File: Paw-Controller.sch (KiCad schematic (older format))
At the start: 26 parts, among them J1 Conn_02x06_Odd_Even, J2 Conn_01x08, J3 Conn_01x02, Q1 DMN1019USN, Q2 DMN1019USN, Q3 DMN1019USN, SW1 SW_SPST_KMR2, U1 LMZ10503, U2 ATSAMD21E18A-AF

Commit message: Added missing PWM labels.
Signed-off-by: Aaron Williams <aaron.w2@gmail.com>
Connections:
- net labels added: PWM0, PWM1, PWM2
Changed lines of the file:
@@
 Wire Notes Line
 	6200 4600 10300 4600
+Text Label 8100 2600 0    50   ~ 0
+PWM0
+Text Label 8100 2700 0    50   ~ 0
+PWM1
+Text Label 8850 3300 0    50   ~ 0
+PWM2
 $EndSCHEMATC

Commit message: Version 2.0 converts each PWM channel to use an H-bridge.
This allows the controller to be able to drive a 3V brushless motor.  The
M0 processor is capable of generating the timing for the motors, though at
this time I don't know if it works with 6 GPIO pins or only with three.

Six was chosen so that a PWMs can be set to a high impedence state.  This
is useful in the case where multiple brushed motors are attached between either
+3v or ground and the PWM pin, though the alternative is to just pull the PWM
output to the same level.  That might be version 2.1 later.

Signed-off-by: Aaron Williams <aaron.w2@gmail.com>
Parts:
- removed D1, D2, D3: B120-E3, Diode_SMD:D_SMA, symbol Diode:B120-E3
- added Q4, Q5, Q6: SI3493DDV-T1-GE3, Package_SO:TSOP-6_1.65x3.05mm_P0.95mm, symbol Aaron:SI3493DDV-T1-GE3
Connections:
- net labels added: PA03, PA04, PA05
- wire segments 85 -> 90
- no-connect marks 14 -> 12
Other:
- note added: "PWM Drivers, 3V Max"
- note removed: "PWM Drivers, 5V Max"
- moved on the sheet: C8, Q1, Q2, Q3, SW1

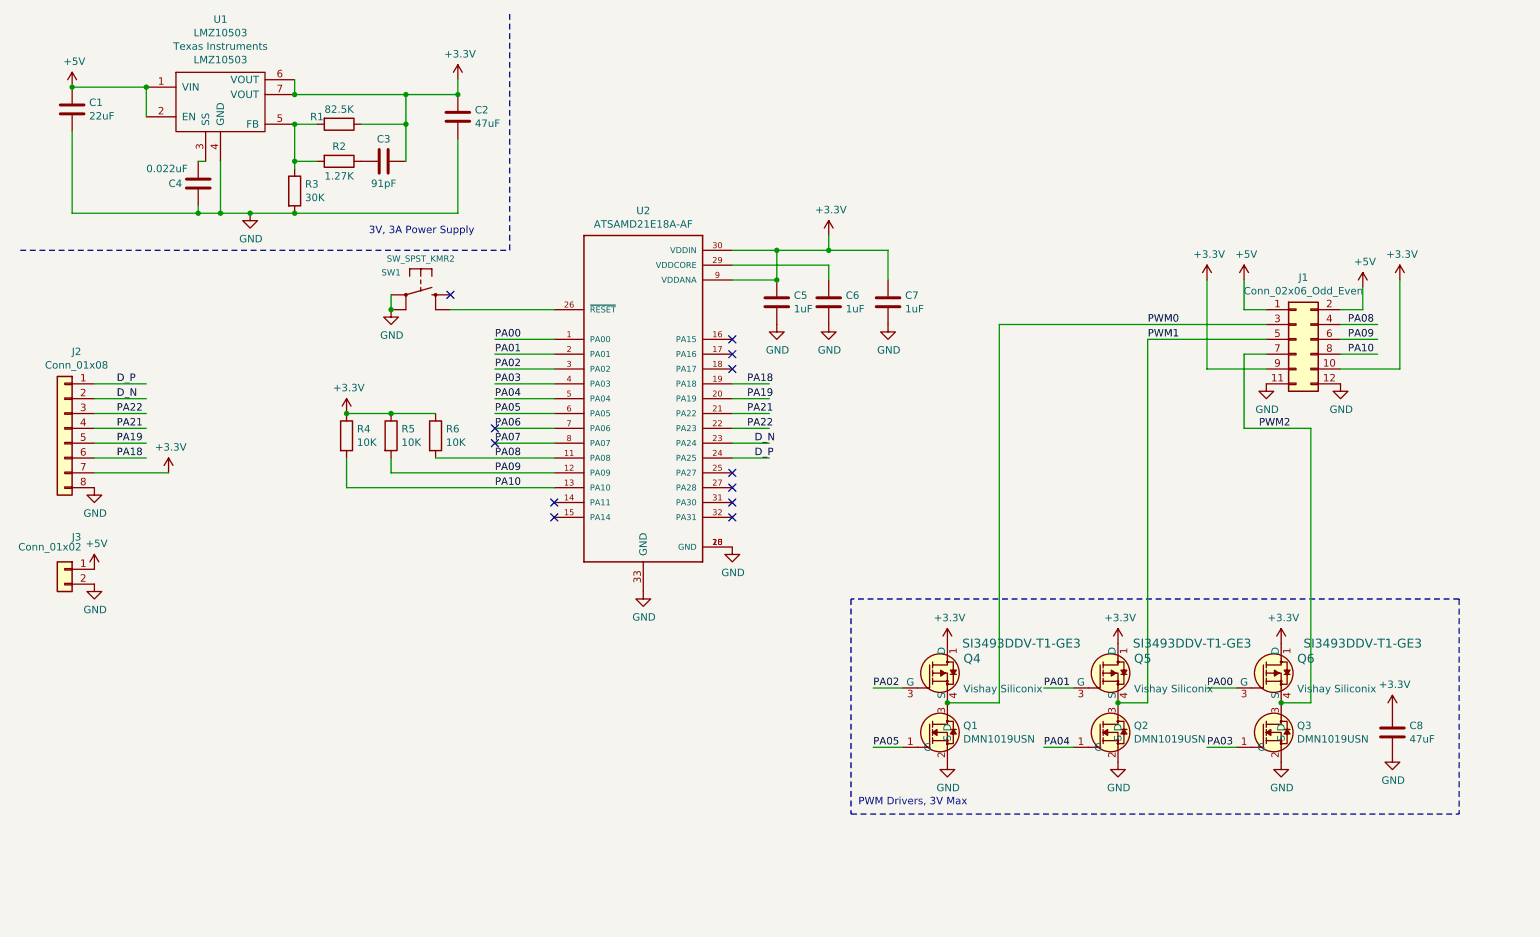
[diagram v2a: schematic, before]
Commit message: Fixed solder mask clearance.
Signed-off-by: Aaron Williams <aaron.w2@gmail.com>
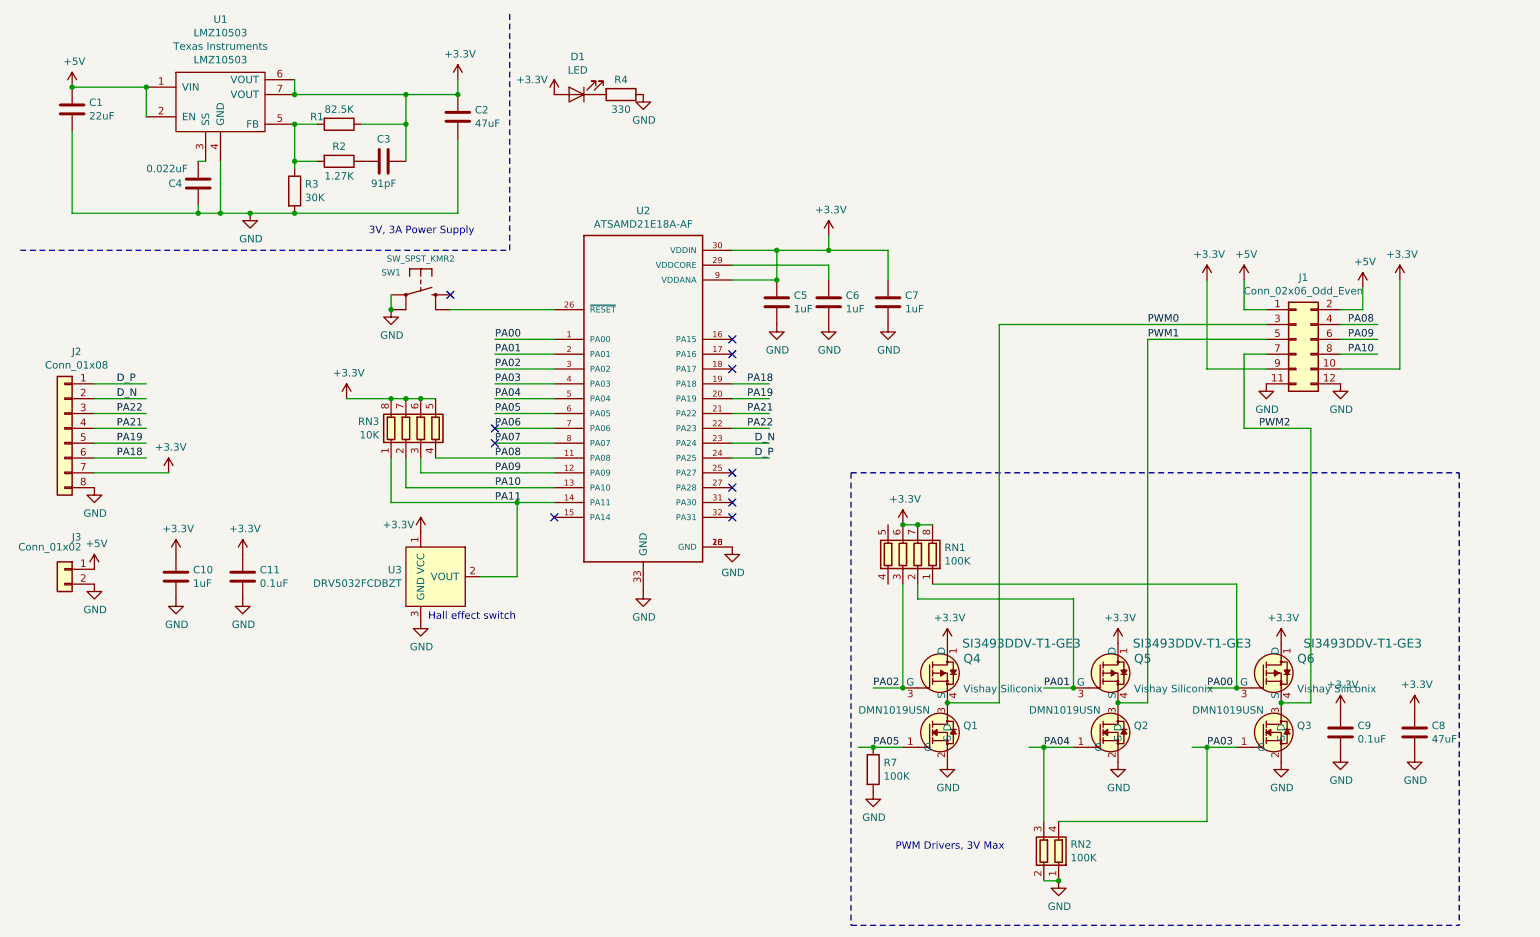
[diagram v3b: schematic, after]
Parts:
- removed R5, R6: 10K, Resistor_SMD:R_0603_1608Metric, symbol Device:R
- added C10: 1uF, Capacitor_SMD:C_0603_1608Metric, symbol Device:C
- added C11, C9: 0.1uF, Capacitor_SMD:C_0603_1608Metric, symbol Device:C
- added D1: LED, LED_SMD:LED_0603_1608Metric, symbol Device:LED
- added R7: 100K, Resistor_SMD:R_0603_1608Metric, symbol Paw-Controller-rescue:R-device
- added RN1: 100K, Resistor_SMD:R_Array_Convex_4x0603, symbol Paw-Controller-rescue:R_Pack04-device
- added RN2: 100K, Resistor_SMD:R_Array_Convex_2x0603, symbol Paw-Controller-rescue:R_Pack02-device
- added RN3: 10K, Resistor_SMD:R_Array_Convex_4x0603, symbol Paw-Controller-rescue:R_Pack04-device
- added U3: DRV5032FCDBZT, Package_TO_SOT_SMD:SOT-23, symbol Aaron:DRV5032FCDBZT
- R4: value 10K -> 330
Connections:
- net labels added: PA11
- wire segments 90 -> 112
- no-connect marks 12 -> 11
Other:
- note added: "Hall effect switch"
- moved on the sheet: C8

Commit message: Fixed P-CH mosfets and changed to more readily available mosfet.
Signed-off-by: Aaron Williams <aaron.w2@gmail.com>
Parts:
- removed Q4, Q5, Q6: SI3493DDV-T1-GE3, Package_SO:TSOP-6_1.65x3.05mm_P0.95mm, symbol Aaron:SI3493DDV-T1-GE3
- added Q? (x3): SI3407DV-T1-GE3, digikey-footprints:SOT-23-3, symbol Aaron:SI3407DV-T1-GE3
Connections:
- wire segments 112 -> 115
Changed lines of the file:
@@
 Sheet 1 1
 Title "3v PWM controller"
-Date "2018-10-16"
-Rev "2.1"
+Date "2019-01-29"
+Rev "2.1.2"
 Comp "Aaron Williams"
 Comment1 ""
@@
 Text Label 8850 3300 0    50   ~ 0
 PWM2
-$Comp
-L Aaron:SI3493DDV-T1-GE3 Q4
-U 1 1 5BC63C22
-P 6750 4950
-F 0 "Q4" H 6858 5048 60  0000 L CNN
-F 1 "SI3493DDV-T1-GE3" H 6850 5150 60  0000 L CNN
-F 2 "Package_SO:TSOP-6_1.65x3.05mm_P0.95mm" H 6950 5150 60  0001 L CNN
-F 3 "http://www.vishay.com/docs/74735/si3493ddv.pdf" H 6950 5250 60  0001 L CNN
-F 4 "Vishay Siliconix" H 6858 4844 50  0000 L CNN "MFR"
-F 5 "SI3493DDV-T1-GE3" H 6950 5450 60  0001 L CNN "MPN"
-F 6 "SI3493DDV-T1-GE3TR-ND" H 6950 5350 60  0001 L CNN "Digi-Key_PN"
-F 7 "Discrete Semiconductor Products" H 6950 5550 60  0001 L CNN "Category"
-F 8 "Transistors - FETs, MOSFETs - Single" H 6950 5650 60  0001 L CNN "Family"
-F 9 "http://www.vishay.com/docs/74735/si3493ddv.pdf" H 6950 5750 60  0001 L CNN "DK_Datasheet_Link"
-F 10 "https://www.digikey.com/product-detail/en/vishay-siliconix/SI3493DDV-T1-GE3/" H 6950 5850 60  0001 L CNN "DK_Detail_Page"
-F 11 "MOSFET P-CH 20V 8A 6TSOP" H 6950 5950 60  0001 L CNN "Description"
-F 12 "Vishay Siliconix" H 6950 6050 60  0001 L CNN "Manufacturer"
-F 13 "Active" H 6950 6150 60  0001 L CNN "Status"
-	1    6750 4950
-	1    0    0    -1
-$EndComp
-$Comp
-L Aaron:SI3493DDV-T1-GE3 Q5
-U 1 1 5BC646E4
-P 7900 4950
-F 0 "Q5" H 8008 5048 60  0000 L CNN
-F 1 "SI3493DDV-T1-GE3" H 8000 5150 60  0000 L CNN
-F 2 "Package_SO:TSOP-6_1.65x3.05mm_P0.95mm" H 8100 5150 60  0001 L CNN
-F 3 "http://www.vishay.com/docs/74735/si3493ddv.pdf" H 8100 5250 60  0001 L CNN
-F 4 "Vishay Siliconix" H 8008 4844 50  0000 L CNN "MFR"
-F 5 "SI3493DDV-T1-GE3" H 8100 5450 60  0001 L CNN "MPN"
-F 6 "SI3493DDV-T1-GE3TR-ND" H 8100 5350 60  0001 L CNN "Digi-Key_PN"
-F 7 "Discrete Semiconductor Products" H 8100 5550 60  0001 L CNN "Category"
-F 8 "Transistors - FETs, MOSFETs - Single" H 8100 5650 60  0001 L CNN "Family"
-F 9 "http://www.vishay.com/docs/74735/si3493ddv.pdf" H 8100 5750 60  0001 L CNN "DK_Datasheet_Link"
-F 10 "https://www.digikey.com/product-detail/en/vishay-siliconix/SI3493DDV-T1-GE3/" H 8100 5850 60  0001 L CNN "DK_Detail_Page"
-F 11 "MOSFET P-CH 20V 8A 6TSOP" H 8100 5950 60  0001 L CNN "Description"
-F 12 "Vishay Siliconix" H 8100 6050 60  0001 L CNN "Manufacturer"
-F 13 "Active" H 8100 6150 60  0001 L CNN "Status"
-	1    7900 4950
-	1    0    0    -1
-$EndComp
-$Comp
-L Aaron:SI3493DDV-T1-GE3 Q6
-U 1 1 5BC647C5
-P 9000 4950
-F 0 "Q6" H 9108 5048 60  0000 L CNN
-F 1 "SI3493DDV-T1-GE3" H 9150 5150 60  0000 L CNN
-F 2 "Package_SO:TSOP-6_1.65x3.05mm_P0.95mm" H 9200 5150 60  0001 L CNN
-F 3 "http://www.vishay.com/docs/74735/si3493ddv.pdf" H 9200 5250 60  0001 L CNN
-F 4 "Vishay Siliconix" H 9108 4844 50  0000 L CNN "MFR"
-F 5 "SI3493DDV-T1-GE3" H 9200 5450 60  0001 L CNN "MPN"
-F 6 "SI3493DDV-T1-GE3TR-ND" H 9200 5350 60  0001 L CNN "Digi-Key_PN"
-F 7 "Discrete Semiconductor Products" H 9200 5550 60  0001 L CNN "Category"
-F 8 "Transistors - FETs, MOSFETs - Single" H 9200 5650 60  0001 L CNN "Family"
-F 9 "http://www.vishay.com/docs/74735/si3493ddv.pdf" H 9200 5750 60  0001 L CNN "DK_Datasheet_Link"
-F 10 "https://www.digikey.com/product-detail/en/vishay-siliconix/SI3493DDV-T1-GE3/" H 9200 5850 60  0001 L CNN "DK_Detail_Page"
-F 11 "MOSFET P-CH 20V 8A 6TSOP" H 9200 5950 60  0001 L CNN "Description"
-F 12 "Vishay Siliconix" H 9200 6050 60  0001 L CNN "Manufacturer"
-F 13 "Active" H 9200 6150 60  0001 L CNN "Status"
-	1    9000 4950
-	1    0    0    -1
-$EndComp
 Wire Wire Line
 	6450 5050 6250 5050
@@
 Wire Wire Line
 	7100 5150 7100 2600
-Connection ~ 6750 5150
 Wire Wire Line
 	7100 2600 8900 2600
@@
 Wire Wire Line
 	8100 5150 8100 2700
-Connection ~ 7900 5150
 Wire Wire Line
 	9000 5150 9200 5150
@@
 Wire Wire Line
 	8750 3300 9200 3300
-Connection ~ 9000 5150
 $Comp
 L power:+3.3V #PWR025
@@
 	-1   0    0    -1
 $EndComp
-Connection ~ 8700 5050
 Wire Wire Line
 	6550 4350 6550 4450
-Wire Wire Line
-	7600 4450 7600 5050
-Connection ~ 7600 5050
-Connection ~ 6450 5050
 Wire Wire Line
 	6250 5450 6450 5450
@@
 $EndComp
 Wire Wire Line
-	8700 4350 8700 5050
-Wire Wire Line
 	6450 3950 6550 3950
 Connection ~ 6450 3950
@@
 Wire Wire Line
 	6550 4450 7600 4450
-Wire Wire Line
-	6450 4350 6450 5050
 Wire Notes Line
 	6100 3600 10200 3600
@@
 Text Notes 3250 4600 0    50   ~ 0
 Hall effect switch
+$Comp
+L Aaron:SI3407DV-T1-GE3 Q?
+U 1 1 5C524C33
+P 6750 4950
+F 0 "Q?" H 6858 4897 60  0000 L CNN
+F 1 "SI3407DV-T1-GE3" H 6550 4750 60  0000 L CNN
+F 2 "digikey-footprints:SOT-23-3" H 6950 5150 60  0001 L CNN
+F 3 "http://www.vishay.com/docs/74735/si3493ddv.pdf" H 6950 5250 60  0001 L CNN
+F 4 "Vishay Siliconix" H 7250 5050 50  0001 C CNN "MFR"
+F 5 "SI3407DV-T1-GE3" H 6950 5450 60  0001 L CNN "MPN"
+F 6 "Digikey" H 6944 5393 50  0001 C CNN "SPR"
+F 7 "SI3407DV-T1-GE3CT-ND" H 7044 5493 50  0001 C CNN "SPN"
+F 8 "https://www.digikey.com/product-detail/en/vishay-siliconix/SI3407DV-T1-GE3/SI3407DV-T1-GE3CT-ND/" H 7144 5593 50  0001 C CNN "SPURL"
+F 9 "SI3407DV-T1-GE3TR-ND" H 6950 5350 60  0001 L CNN "Digi-Key_PN"
+F 10 "Discrete Semiconductor Products" H 6950 5550 60  0001 L CNN "Category"
+F 11 "Transistors - FETs, MOSFETs - Single" H 6950 5650 60  0001 L CNN "Family"
+F 12 "http://www.vishay.com/docs/69987/si3407dv.pdf" H 6950 5750 60  0001 L CNN "DK_Datasheet_Link"
+F 13 "https://www.digikey.com/product-detail/en/vishay-siliconix/SI3407DV-T1-GE3/SI3407DV-T1-GE3CT-ND/" H 6950 5850 60  0001 L CNN "DK_Detail_Page"
+F 14 "MOSFET P-CH 20V 8A 6TSOP" H 6950 5950 60  0001 L CNN "Description"
+F 15 "Vishay Siliconix" H 6950 6050 60  0001 L CNN "Manufacturer"
+F 16 "Active" H 6950 6150 60  0001 L CNN "Status"
+	1    6750 4950
+	1    0    0    1
+$EndComp
+Wire Wire Line
+	6450 4350 6450 4850
+Connection ~ 6450 4850
+Wire Wire Line
+	6450 4850 6450 5050
+Connection ~ 6750 5150
+Wire Wire Line
+	7600 4450 7600 4850
+$Comp
+L Aaron:SI3407DV-T1-GE3 Q?
+U 1 1 5C534FFC
+P 7900 4950
+F 0 "Q?" H 8008 4897 60  0000 L CNN
+F 1 "SI3407DV-T1-GE3" H 7700 4750 60  0000 L CNN
+F 2 "digikey-footprints:SOT-23-3" H 8100 5150 60  0001 L CNN
+F 3 "http://www.vishay.com/docs/74735/si3493ddv.pdf" H 8100 5250 60  0001 L CNN
+F 4 "Vishay Siliconix" H 8400 5050 50  0001 C CNN "MFR"
+F 5 "SI3407DV-T1-GE3" H 8100 5450 60  0001 L CNN "MPN"
+F 6 "Digikey" H 8094 5393 50  0001 C CNN "SPR"
+F 7 "SI3407DV-T1-GE3CT-ND" H 8194 5493 50  0001 C CNN "SPN"
+F 8 "https://www.digikey.com/product-detail/en/vishay-siliconix/SI3407DV-T1-GE3/SI3407DV-T1-GE3CT-ND/" H 8294 5593 50  0001 C CNN "SPURL"
+F 9 "SI3407DV-T1-GE3TR-ND" H 8100 5350 60  0001 L CNN "Digi-Key_PN"
+F 10 "Discrete Semiconductor Products" H 8100 5550 60  0001 L CNN "Category"
+F 11 "Transistors - FETs, MOSFETs - Single" H 8100 5650 60  0001 L CNN "Family"
+F 12 "http://www.vishay.com/docs/69987/si3407dv.pdf" H 8100 5750 60  0001 L CNN "DK_Datasheet_Link"
+F 13 "https://www.digikey.com/product-detail/en/vishay-siliconix/SI3407DV-T1-GE3/SI3407DV-T1-GE3CT-ND/" H 8100 5850 60  0001 L CNN "DK_Detail_Page"
+F 14 "MOSFET P-CH 20V 8A 6TSOP" H 8100 5950 60  0001 L CNN "Description"
+F 15 "Vishay Siliconix" H 8100 6050 60  0001 L CNN "Manufacturer"
+F 16 "Active" H 8100 6150 60  0001 L CNN "Status"
+	1    7900 4950
+	1    0    0    1
+$EndComp
+Connection ~ 7900 5150
+Connection ~ 7600 4850
+Wire Wire Line
+	7600 4850 7600 5050
+Wire Wire Line
+	8700 4350 8700 4850
+$Comp
+L Aaron:SI3407DV-T1-GE3 Q?
+U 1 1 5C535C5D
+P 9000 4950
+F 0 "Q?" H 9108 4897 60  0000 L CNN
+F 1 "SI3407DV-T1-GE3" H 8800 4750 60  0000 L CNN
+F 2 "digikey-footprints:SOT-23-3" H 9200 5150 60  0001 L CNN
+F 3 "http://www.vishay.com/docs/74735/si3493ddv.pdf" H 9200 5250 60  0001 L CNN
+F 4 "Vishay Siliconix" H 9500 5050 50  0001 C CNN "MFR"
+F 5 "SI3407DV-T1-GE3" H 9200 5450 60  0001 L CNN "MPN"
+F 6 "Digikey" H 9194 5393 50  0001 C CNN "SPR"
+F 7 "SI3407DV-T1-GE3CT-ND" H 9294 5493 50  0001 C CNN "SPN"
+F 8 "https://www.digikey.com/product-detail/en/vishay-siliconix/SI3407DV-T1-GE3/SI3407DV-T1-GE3CT-ND/" H 9394 5593 50  0001 C CNN "SPURL"
+F 9 "SI3407DV-T1-GE3TR-ND" H 9200 5350 60  0001 L CNN "Digi-Key_PN"
+F 10 "Discrete Semiconductor Products" H 9200 5550 60  0001 L CNN "Category"
+F 11 "Transistors - FETs, MOSFETs - Single" H 9200 5650 60  0001 L CNN "Family"
+F 12 "http://www.vishay.com/docs/69987/si3407dv.pdf" H 9200 5750 60  0001 L CNN "DK_Datasheet_Link"
+F 13 "https://www.digikey.com/product-detail/en/vishay-siliconix/SI3407DV-T1-GE3/SI3407DV-T1-GE3CT-ND/" H 9200 5850 60  0001 L CNN "DK_Detail_Page"
+F 14 "MOSFET P-CH 20V 8A 6TSOP" H 9200 5950 60  0001 L CNN "Description"
+F 15 "Vishay Siliconix" H 9200 6050 60  0001 L CNN "Manufacturer"
+F 16 "Active" H 9200 6150 60  0001 L CNN "Status"
+	1    9000 4950
+	1    0    0    1
+$EndComp
+Connection ~ 9000 5150
+Connection ~ 8700 4850
+Wire Wire Line
+	8700 4850 8700 5050
 $EndSCHEMATC

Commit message: Add another push/pull channel
This adds a 4th push/pull channel and exports PA17 to J1.

Due to the increase in board size, two more pins were added to J2,
an additional +5 and ground pin for USB.

Updated to version 2.2.0

Signed-off-by: Aaron Williams <aaron.w2@gmail.com>
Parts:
- removed J1: Conn_02x06_Odd_Even, Connector_PinHeader_2.54mm:PinHeader_2x06_P2.54mm_Vertical, symbol Connector_Generic:Conn_02x06_Odd_Even
- removed J2: Conn_01x08, Connector_PinHeader_2.54mm:PinHeader_1x08_P2.54mm_Vertical, symbol Connector_Generic:Conn_01x08
- removed R7: 100K, Resistor_SMD:R_0603_1608Metric, symbol Paw-Controller-rescue:R-device
- removed RN2: 100K, Resistor_SMD:R_Array_Convex_2x0603, symbol Paw-Controller-rescue:R_Pack02-device
- added J1: Conn_02x07_Odd_Even, Connector_PinHeader_2.54mm:PinHeader_2x07_P2.54mm_Vertical, symbol Connector_Generic:Conn_02x07_Odd_Even
- added J2: Conn_01x10, Connector_PinHeader_2.54mm:PinHeader_1x10_P2.54mm_Vertical, symbol Connector_Generic:Conn_01x10
- added Q7: SI3407DV-T1-GE3, Package_SO:TSOP-6_1.65x3.05mm_P0.95mm, symbol Aaron:SI3407DV-T1-GE3
- added Q8: DMN1019USN, Package_TO_SOT_SMD:SOT-23, symbol Aaron:DMN1019USN
- added RN2: 100K, Resistor_SMD:R_Array_Convex_4x0603, symbol Paw-Controller-rescue:R_Pack04-device
- Q4, Q5, Q6: renamed from Q?; footprint digikey-footprints:SOT-23-3 -> Package_SO:TSOP-6_1.65x3.05mm_P0.95mm
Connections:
- net labels added: PA17, PWM3
- wire segments 115 -> 138
- no-connect marks 11 -> 8
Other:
- moved on the sheet: C8, C9, RN1
